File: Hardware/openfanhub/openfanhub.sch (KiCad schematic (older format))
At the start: 13 parts, among them J1 Conn_01x04_Male, J2 Conn_01x04_Male, J3 Conn_01x04_Male, U1 STM32F103C8T8_Board, U2 AMS1117, U3 USB_HEADER_IN, U4 USB_HEADER_OUT

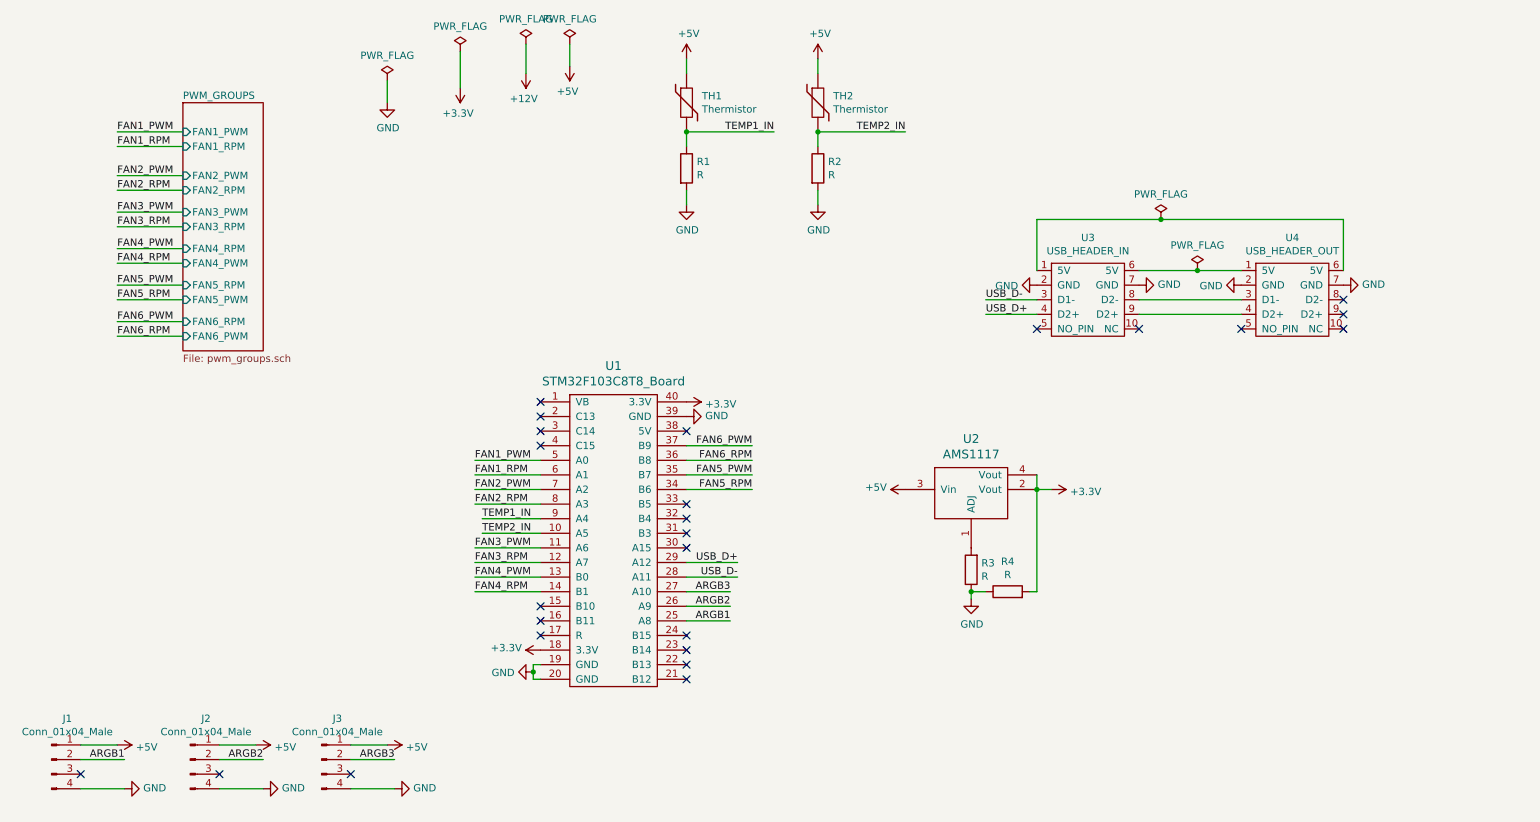
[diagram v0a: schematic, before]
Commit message: Update schematics with new pin layout
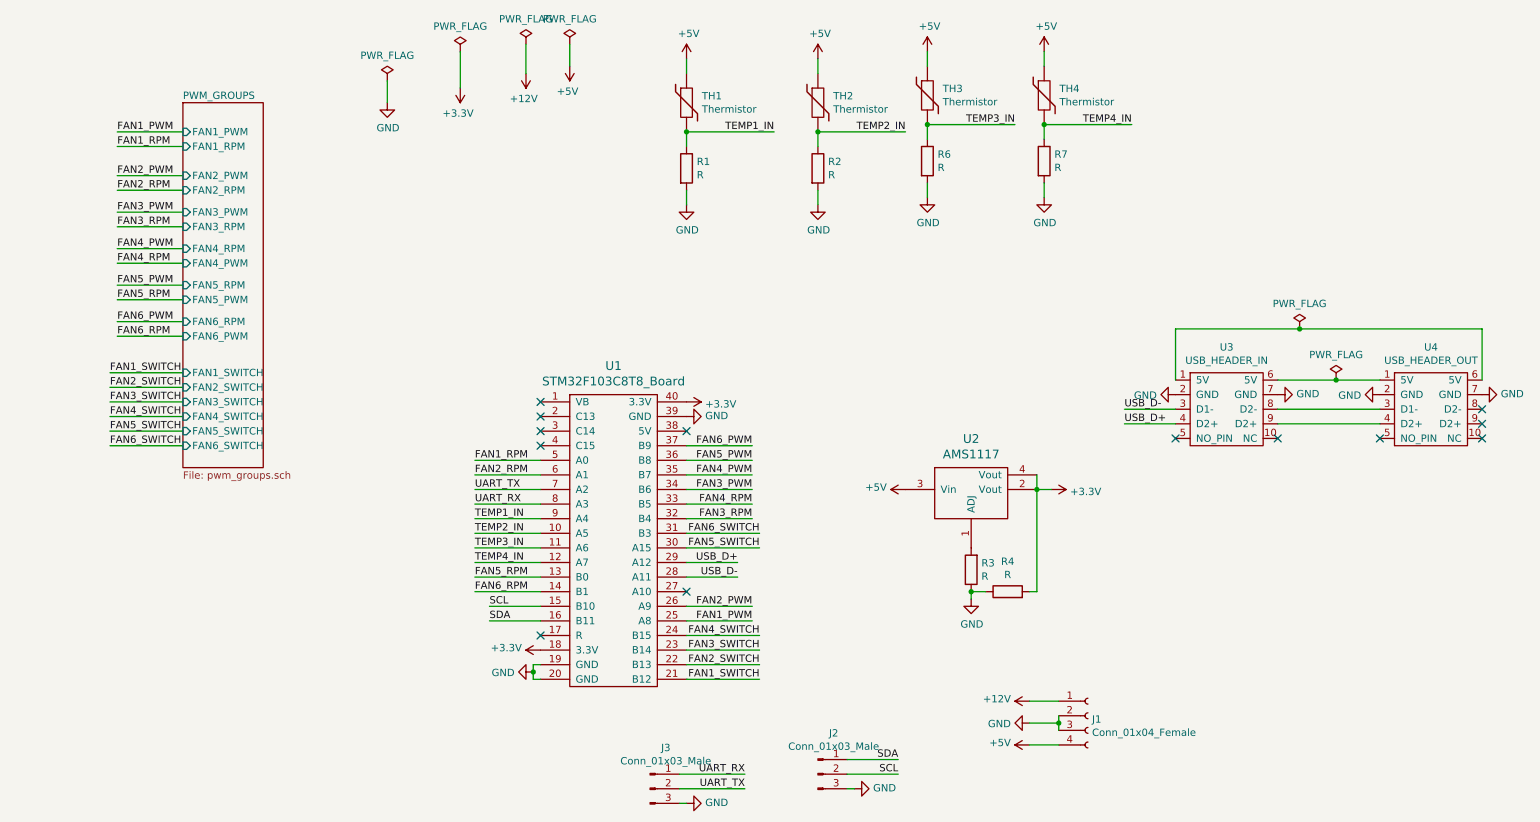
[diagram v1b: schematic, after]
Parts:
- removed J1, J2, J3: Conn_01x04_Male, Connector_PinHeader_2.54mm:PinHeader_1x04_P2.54mm_Horizontal, symbol Connector:Conn_01x04_Male
- added J1: Conn_01x04_Female, symbol Connector:Conn_01x04_Female
- added J2, J3: Conn_01x03_Male, symbol Connector:Conn_01x03_Male
- added R6, R7: R, Resistor_SMD:R_0805_2012Metric, symbol Device:R
- added TH3, TH4: Thermistor, Connector_PinHeader_2.54mm:PinHeader_1x02_P2.54mm_Horizontal, symbol Device:Thermistor
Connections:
- net ARGB1 is gone; now on net FAN1_PWM: U1.25 (A8)
- net ARGB2 is gone; now on net FAN2_PWM: U1.26 (A9)
- net +12V: now also J1.1 (Pin_1)
- net +5V: now also J1.4 (Pin_4), TH3.1, TH4.1
- net FAN1_PWM: no longer U1.5 (A0)
- net FAN1_RPM: now also U1.5 (A0); no longer U1.6 (A1)
- net FAN2_PWM: no longer U1.7 (A2)
- net FAN2_RPM: now also U1.6 (A1); no longer U1.8 (A3)
- net FAN3_PWM: now also U1.34 (B6); no longer U1.11 (A6)
- net FAN3_RPM: now also U1.32 (B4); no longer U1.12 (A7)
- net FAN4_PWM: now also U1.35 (B7); no longer U1.13 (B0)
- net FAN4_RPM: now also U1.33 (B5); no longer U1.14 (B1)
- net FAN5_PWM: now also U1.36 (B8); no longer U1.35 (B7)
- net FAN5_RPM: now also U1.13 (B0); no longer U1.34 (B6)
- net FAN6_RPM: now also U1.14 (B1); no longer U1.36 (B8)
- net GND: now also J1.2 (Pin_2), J1.3 (Pin_3), J2.3 (Pin_3), J3.3 (Pin_3), R6.2, R7.2
- net SCL: now reaches U1.15 (B10)
- net SCL: now also J2.2 (Pin_2)
- net SDA: now reaches U1.16 (B11)
- net SDA: now also J2.1 (Pin_1)
- net FAN1_SWITCH: now reaches U1.21 (B12)
- net FAN2_SWITCH: now reaches U1.22 (B13)
- net FAN3_SWITCH: now reaches U1.23 (B14)
- net FAN4_SWITCH: now reaches U1.24 (B15)
- net FAN5_SWITCH: now reaches U1.30 (A15)
- net FAN6_SWITCH: now reaches U1.31 (B3)
- net ARGB3: no longer names the net of U1.27 (A10)
- new net TEMP3_IN: R6.1, TH3.2, U1.11 (A6)
- new net TEMP4_IN: R7.1, TH4.2, U1.12 (A7)
- new net UART_RX: J3.1 (Pin_1), U1.8 (A3)
- new net UART_TX: J3.2 (Pin_2), U1.7 (A2)
- no-connect marks 25 -> 13
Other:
- moved on the sheet: U3, U4

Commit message: Update files to kicad 6
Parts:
- added C1, C2, C3, C4: C, Capacitor_SMD:C_0603_1608Metric, symbol Device:C
- J1: renamed from J3; footprint (none) -> Connector_PinHeader_2.54mm:PinHeader_1x03_P2.54mm_Vertical
- J2: footprint (none) -> Connector_PinHeader_2.54mm:PinHeader_1x03_P2.54mm_Vertical
- J3: renamed from J1; footprint (none) -> Connector_PinHeader_2.54mm:PinHeader_1x04_P2.54mm_Vertical
- renumbered R6 to R3, R3 to R4, R4 to R5, R7 to R6
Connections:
- net +5V: now also R1.1, R2.1, R3.1, R6.1; no longer TH1.1, TH2.1, TH3.1, TH4.1
- net GND: now also TH1.2, TH2.2, TH3.2, TH4.2, C1.2, C2.2, C3.2, C4.2; no longer R1.2, R2.2, R3.2, R6.2
- net TEMP1_IN: now also R1.2, TH1.1, C1.1; no longer R1.1, TH1.2
- net TEMP2_IN: now also R2.2, TH2.1, C2.1; no longer R2.1, TH2.2
- net TEMP3_IN: now also R3.2, TH3.1, C3.1; no longer R3.1, TH3.2
- net TEMP4_IN: now also R6.2, TH4.1, C4.1; no longer R6.1, TH4.2
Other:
- moved on the sheet: R1, R2, R3, R6, TH1, TH2, TH3, TH4
